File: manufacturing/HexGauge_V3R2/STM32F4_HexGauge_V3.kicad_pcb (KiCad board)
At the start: 4 copper layers, 49.8 x 44.2 mm, 75 parts, among them J1 USB_B_Micro, J3 Micro_SD_Card, J4 Conn_01x04_Pin, J5 Conn_02x05_Odd_Even, Q1 Q_PMOS_GSD, SW1 SW_Omron_B3FS, SW2 SW_SPDT, U1 STM32F405RGT6, U2 TPMP2359D, U3 SN65HVD230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

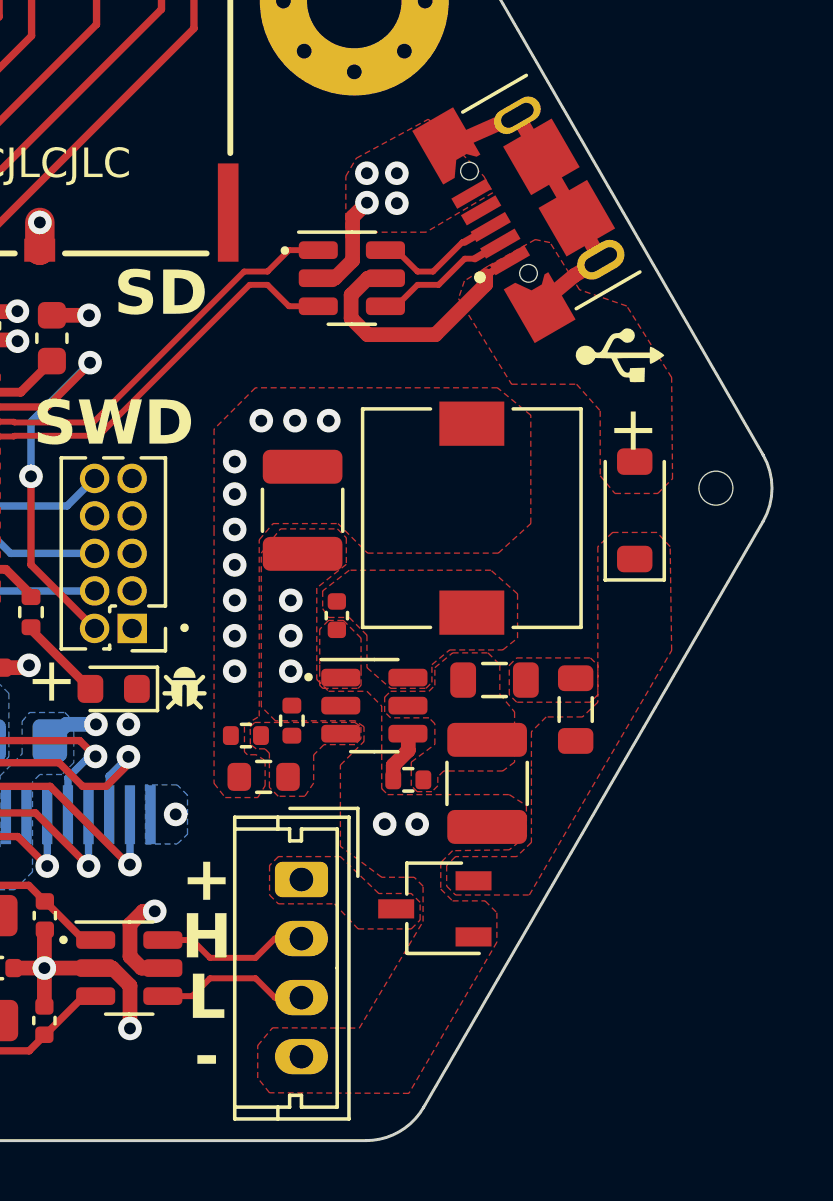
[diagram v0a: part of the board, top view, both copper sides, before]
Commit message: Started Board Rev3
Optimize Component Costs
Smaller Buck Converter ->
Move STM32 3mm to the right to simplify SD Card, IMU, TFT routing
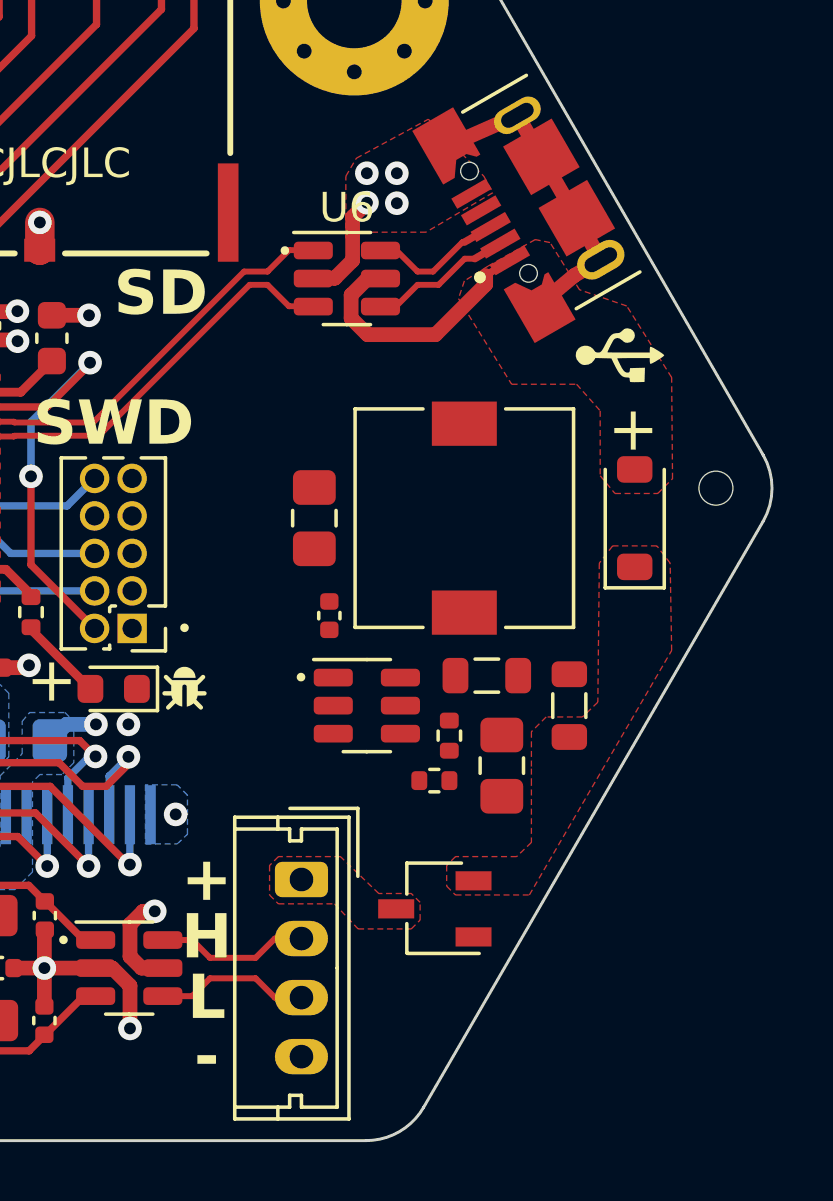
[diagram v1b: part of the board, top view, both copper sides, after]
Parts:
- removed R11: 10k, Resistor_SMD:R_0402_1005Metric
- removed R8: 33k, Resistor_SMD:R_0402_1005Metric
- removed R9: 560k, Resistor_SMD:R_0603_1608Metric
- added R18: 100k, Resistor_SMD:R_0402_1005Metric, F.Cu at (135.4, 93.7)
- C14: value 22n -> 2u2; footprint Capacitor_SMD:C_0402_1005Metric -> Capacitor_SMD:C_0805_2012Metric_Pad1.18x1.45mm_HandSolder
- C15: value 47u -> 10u; footprint Capacitor_SMD:C_1210_3225Metric -> Capacitor_SMD:C_0805_2012Metric_Pad1.18x1.45mm_HandSolder
- C16: value 47u -> 100n; footprint Capacitor_SMD:C_1210_3225Metric -> Capacitor_SMD:C_0402_1005Metric
- L1: value 4u7 -> 3u3
- SW1: value SW_Omron_B3FS -> SW_Panasonic_EVQPUC
- U2: value TPMP2359D -> LMR16006YQ3; footprint Package_TO_SOT_SMD:TSOT-23-6 -> Package_TO_SOT_SMD:SOT-23-6
- U6: value USBLC6-4 -> USBLC6-2
- moved C16 7.80 mm to (131.8, 88.1), turned to 90 degrees
- moved C14 7.55 mm to (137.7, 93.2), turned to -90 degrees
- moved R10 2.04 mm to (135.9, 92.2), turned to -90 degrees
- moved C15 0.48 mm to (131.3, 84.8)
- moved FB1 0.30 mm to (137.2, 90.2)
- moved D2 0.27 mm to (142.2, 84.8)
- moved F1 0.25 mm to (140.0, 91.2)
- moved L1 0.25 mm to (136.4, 84.8)
- moved U2 0.25 mm to (133.1, 91.2)
- moved U6 0.17 mm to (132.4, 76.7)
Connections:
- C14 pad 1: /PMU/BUCK_BST -> /PMU/BUCK_IN
- C14 pad 2: /PMU/BUCK_OUT -> GND
- C15 pad 1: +3V3 -> +3.3V
- C16 pad 1: /PMU/BUCK_IN -> /PMU/BUCK_BST
- C16 pad 2: GND -> /PMU/BUCK_OUT
- L1 pad 2: +3V3 -> +3.3V
- U2 pad 3: /PMU/BUCK_FB -> +3.3V
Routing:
- net /PMU/BUCK_EN: track 1.78 -> 0.00 mm
- net GND: vias 40 -> 35
- net +3V3: vias 28 -> 18
- removed copper zone on F.Cu, net +3V3
- removed copper zone on F.Cu, net /PMU/BUCK_BST
- removed copper zone on F.Cu, net /PMU/BUCK_FB
- removed copper zone on F.Cu, net /PMU/BUCK_IN
- removed copper zone on F.Cu, net /PMU/BUCK_OUT
- removed copper zone on F.Cu, net /PMU/POST_FUSE

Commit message: upd board
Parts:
- moved C24 3.61 mm to (113.3, 96.3), turned to 90 degrees
- moved R2 2.81 mm to (109.4, 78.8)
- moved R7 2.70 mm to (113.9, 73.6), turned to 0 degrees
- moved R6 2.57 mm to (111.9, 73.6), turned to 180 degrees
- moved C2 2.53 mm to (108.9, 80.6), turned to -90 degrees
- moved C13 2.50 mm to (124.7, 77.7)
- moved G*** 2.50 mm to (129.4, 90.6)
- moved J5 2.41 mm to (127.5, 88.4)
- moved D1 2.40 mm to (126.9, 90.6)
- moved R5 2.40 mm to (123.9, 87.1)
- moved C6 2.39 mm to (122.7, 78.2)
- moved R16 2.32 mm to (112.1, 96.3), turned to -90 degrees
- moved C7 2.30 mm to (108.9, 85.8)
- moved C4 2.18 mm to (112.9, 91.3)
- moved U1 2.17 mm to (116.4, 83.8)
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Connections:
- U1 pad 50: SD_DET -> unconnected-(U1-PA15-Pad50)
- U1 pad 56: unconnected-(U1-PB4-Pad56) -> SD_DET
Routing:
- net NRST: track 26.7 -> 16.5 mm
- net VBUS: track 8.95 -> 0.97 mm
- net GND: track 75.3 -> 67.4 mm, vias 35 -> 30
- net +3V3: track 45.9 -> 40.6 mm, vias 18 -> 15
- net BTN: track 5.22 -> 0.00 mm
- net SD_DAT3: track 21.1 -> 16.0 mm
- net IMU_INT: track 14.9 -> 19.0 mm
- net /Sensors/CAN_RS: track 3.12 -> 0.00 mm
- net /MCU/VCAP_2: track 2.94 -> 0.00 mm
- net Net-(D1-A): track 2.92 -> 0.00 mm
- net Net-(SW2-B): track 2.15 -> 4.84 mm
- net TFT_CS: track 14.9 -> 12.3 mm
- net IMU_SCL: track 6.33 -> 8.85 mm, vias 0 -> 2
- net TFT_MOSI: track 17.6 -> 15.1 mm
- net TFT_RST: track 18.5 -> 16.1 mm
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- removed copper zone on F.Cu, net +12V
- removed copper zone on B.Cu, net +3V3
- removed copper zone on F.Cu, net /PMU/POST_POL

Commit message: FInalised Revision 2 Design
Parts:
- F1: footprint Inductor_SMD:L_0805_2012Metric -> Inductor_SMD:L_1206_3216Metric
- J1: footprint Connector_USB:USB_Micro-B_XKB_U254-051T-4BH83-F1S -> SamacSys_Parts:101181920002LF
- moved G*** 6.35 mm to (135.3, 79.4)
- moved F1 4.34 mm to (141.9, 87.3)
- moved D2 2.53 mm to (141.9, 82.3)
- moved R18 0.97 mm to (134.4, 93.6)
- moved J1 0.71 mm to (138.6, 74.2)
- moved U6 0.56 mm to (132.4, 77.1)
- moved C26 0.25 mm to (109.9, 74.3)
- moved C13 0.23 mm to (124.9, 77.8)
- moved C14 0.15 mm to (137.7, 93.1)
- moved C15 0.15 mm to (131.2, 84.8)
- moved U2 0.14 mm to (133.2, 91.1)
- moved R10 0.14 mm to (135.9, 92.1)
- moved C16 0.12 mm to (131.9, 88.1)
- moved FB1 0.10 mm to (137.2, 90.1)
- moved C24 0.10 mm to (113.4, 96.3)
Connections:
- C15 pad 1: +3.3V -> +3V3
- L1 pad 2: +3.3V -> +3V3
- U2 pad 3: +3.3V -> +3V3
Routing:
- net NRST: track 16.5 -> 29.1 mm
- net unconnected-(J1-Shield-Pad6): track 10.8 -> 0.00 mm
- net BTN: track 0.00 -> 7.39 mm
- net VBUS: track 0.97 -> 8.09 mm
- net +3V3: track 40.6 -> 47.7 mm, vias 15 -> 28
- net GND: track 67.4 -> 73.2 mm, vias 30 -> 44
- net /Sensors/CAN_RS: track 0.00 -> 5.06 mm
- net /MCU/VCAP_2: track 0.00 -> 3.92 mm
- net Net-(D1-A): track 0.00 -> 3.91 mm
- net +12V: track 0.00 -> 3.21 mm
- net /MCU/DEBUG_LED: track 0.00 -> 1.83 mm
- net IMU_INT: track 19.0 -> 20.0 mm
- net USB_D+: track 13.2 -> 12.5 mm
- net USB_D-: track 13.2 -> 12.5 mm
- net IMU_SCL: track 8.85 -> 8.23 mm
- added copper zone on B.Cu, net +3V3
- added copper zone on F.Cu, net +3V3
- added copper zone on F.Cu, net /PMU/BUCK_BST
- added copper zone on F.Cu, net /PMU/BUCK_EN
- added copper zone on F.Cu, net /PMU/BUCK_IN
- added copper zone on F.Cu, net /PMU/BUCK_OUT
- added copper zone on F.Cu, net /PMU/POST_FUSE
- added copper zone on F.Cu, net /PMU/POST_POL

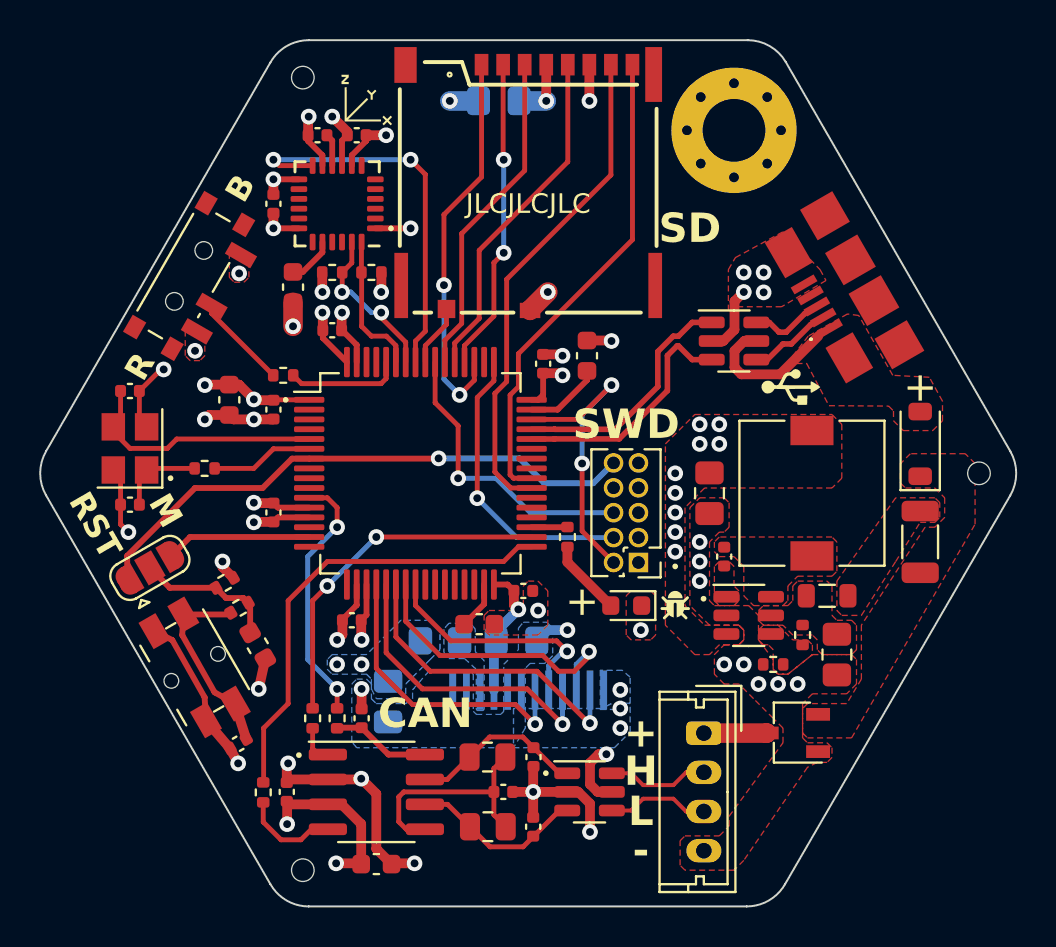
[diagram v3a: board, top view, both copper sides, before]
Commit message: upd board
Small cleanups
- better XTAL isolation
- STM32: lower inductance supply
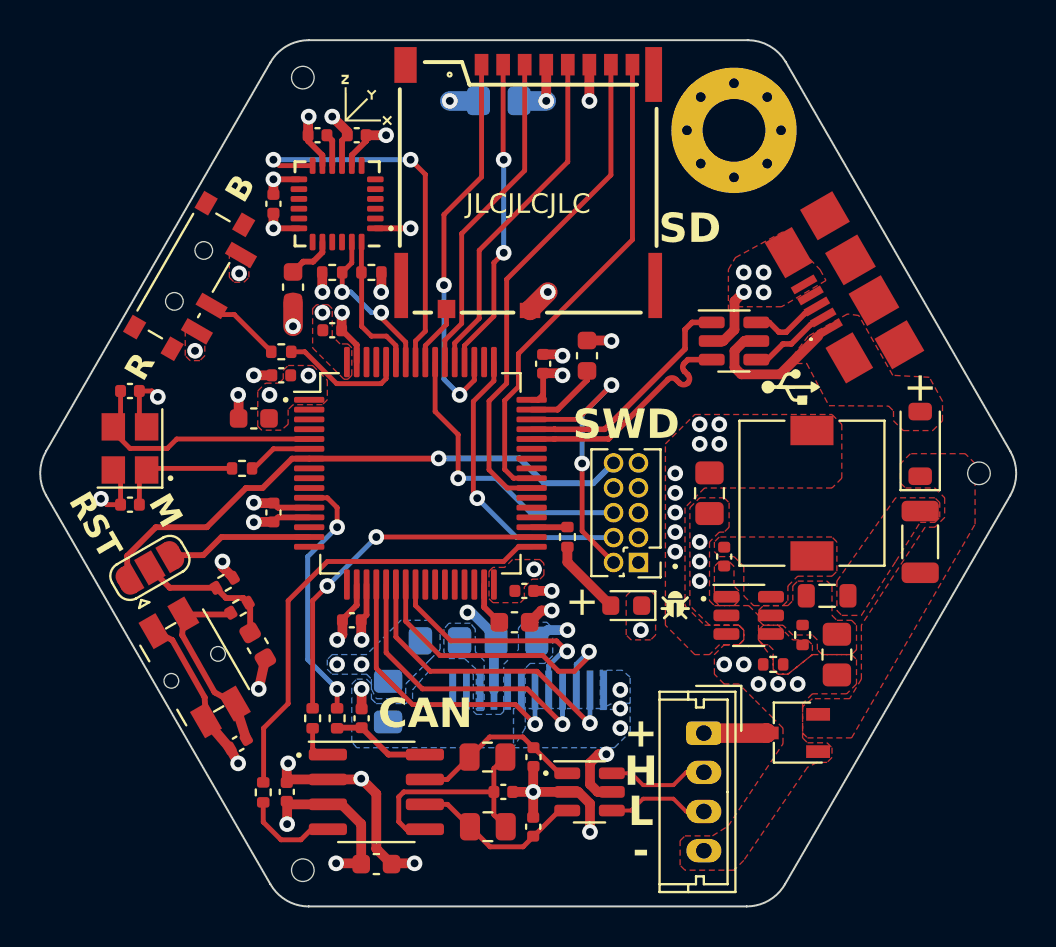
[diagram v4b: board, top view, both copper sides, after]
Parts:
- moved R4 1.91 mm to (107.3, 83.6)
- moved C12 1.80 mm to (121.2, 91.4)
- moved C2 1.80 mm to (109.3, 78.8), turned to 180 degrees
- moved C1 1.57 mm to (107.9, 81.0), turned to 180 degrees
- moved R2 1.20 mm to (109.3, 77.6)
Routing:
- net +3V3: track 47.7 -> 37.0 mm, vias 28 -> 29
- net /MCU/XTAL_IN: track 4.53 -> 6.44 mm
- net /MCU/HSE_OUT: track 5.24 -> 3.33 mm
- net GND: track 73.2 -> 74.2 mm, vias 44 -> 45
- net Net-(SW2-B): track 4.84 -> 4.02 mm
- net /MCU/BOOT0: track 5.86 -> 6.46 mm
- net USB_D-: track 12.5 -> 12.0 mm
